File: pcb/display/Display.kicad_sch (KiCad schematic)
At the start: 32 parts, among them J101 RJ45, J102 Screw Terminal 3.5mm, J103 01x08_Pin, P101 USB_C_Plug_USB2.0, Q101 2N7002, SW101 SW_4x3mm, SW102 SW_4x3mm, SW103 SW_4x3mm, SW104 SW_4x3mm, U101 TMP1075DSGR, U102 ESP32-S3-MINI-1U-N8

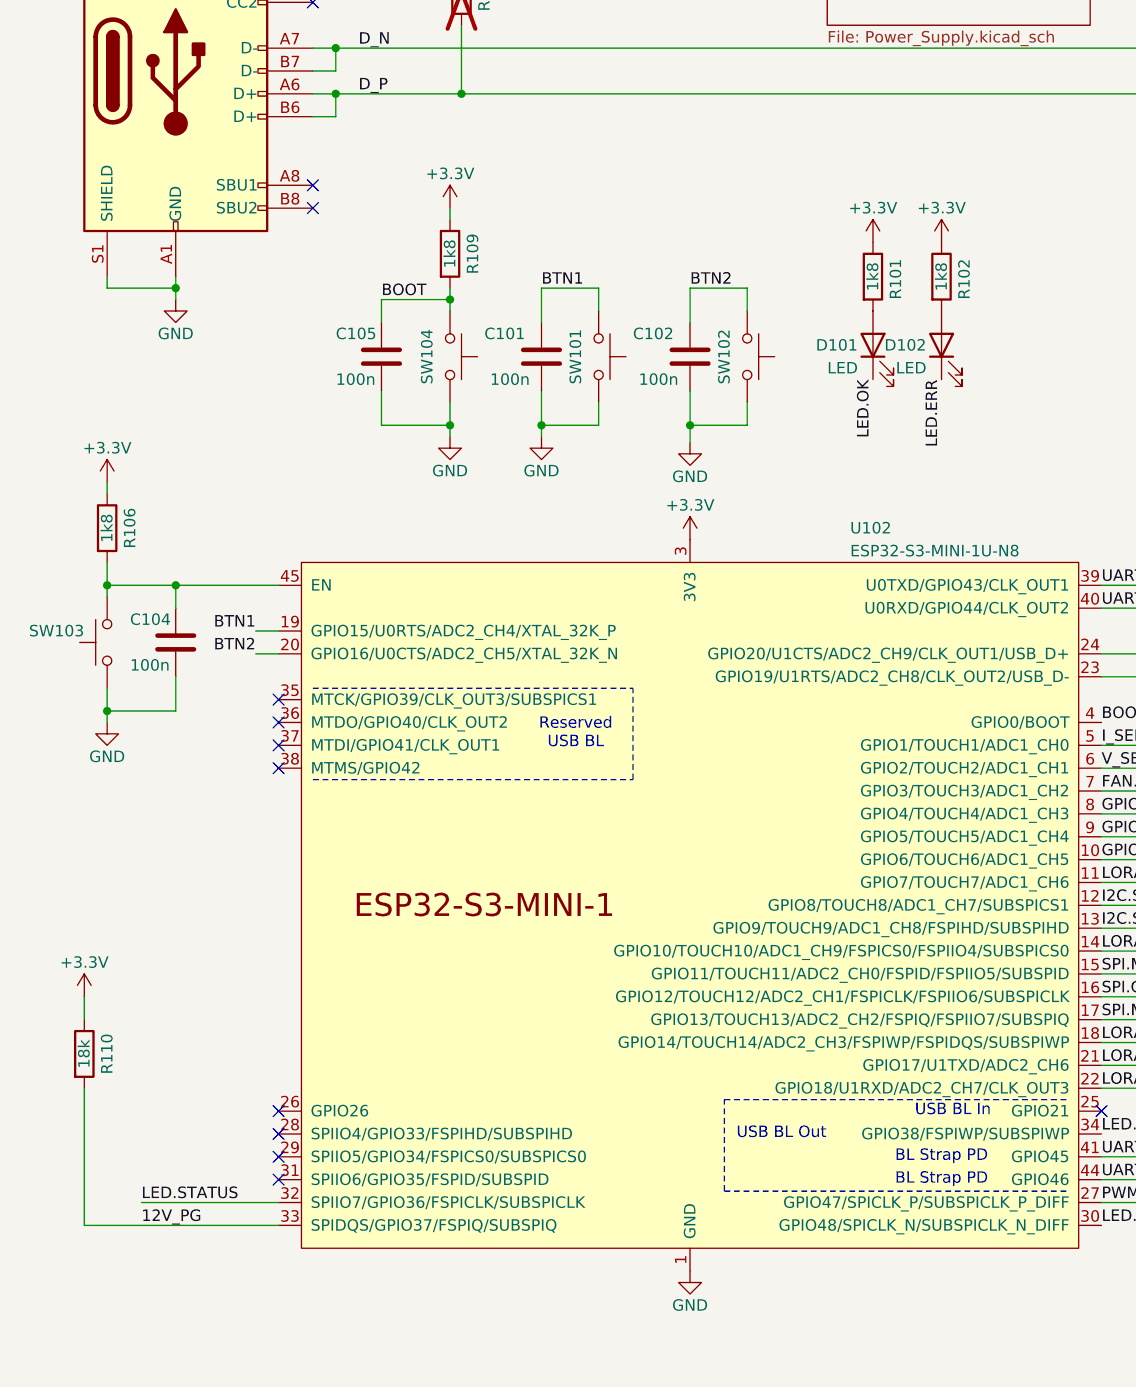
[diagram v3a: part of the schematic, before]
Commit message: Update some wrong values after import in JLC for production
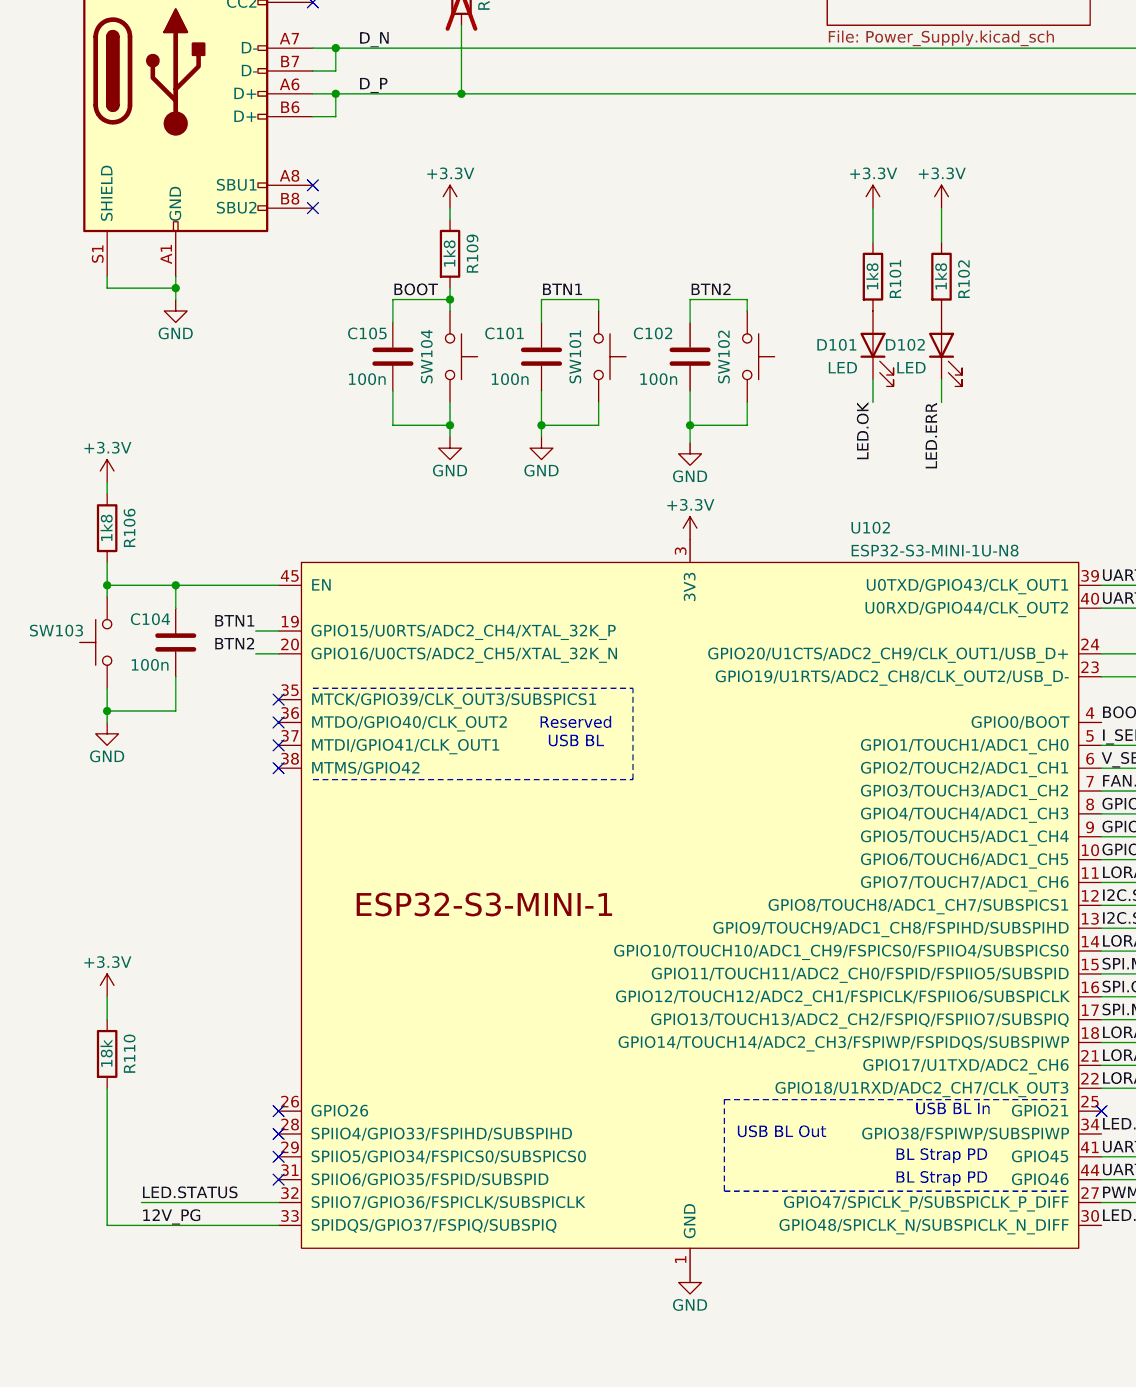
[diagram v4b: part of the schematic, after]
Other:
- moved on the sheet: C105, R110
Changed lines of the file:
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@@
 	(title_block
 		(title "Open Shot Clock - Display")
-		(date "2025-04-08")
+		(date "2025-04-11")
 		(rev "01")
 		(company "Ravenspark")
@@
 	(wire
 		(pts
-			(xy 52.07 71.12) (xy 52.07 68.58)
+			(xy 53.34 71.12) (xy 53.34 68.58)
 		)
 		(stroke
@@
 	(wire
 		(pts
-			(xy 19.05 171.45) (xy 40.64 171.45)
+			(xy 21.59 171.45) (xy 40.64 171.45)
 		)
 		(stroke
@@
 	(wire
 		(pts
-			(xy 86.36 71.12) (xy 86.36 67.31)
+			(xy 86.36 71.12) (xy 86.36 68.58)
 		)
 		(stroke
@@
 	(wire
 		(pts
-			(xy 69.85 67.31) (xy 69.85 71.12)
+			(xy 69.85 68.58) (xy 69.85 71.12)
 		)
 		(stroke
@@
 	(wire
 		(pts
+			(xy 106.68 58.42) (xy 106.68 62.23)
+		)
+		(stroke
+			(width 0)
+			(type default)
+		)
+	)
+	(wire
+		(pts
 			(xy 59.69 80.01) (xy 59.69 82.55)
 		)
@@
 	(wire
 		(pts
+			(xy 114.3 80.01) (xy 114.3 77.47)
+		)
+		(stroke
+			(width 0)
+			(type default)
+		)
+	)
+	(wire
+		(pts
 			(xy 146.05 110.49) (xy 132.08 110.49)
 		)
@@
 	(wire
 		(pts
-			(xy 76.2 67.31) (xy 69.85 67.31)
+			(xy 76.2 68.58) (xy 69.85 68.58)
 		)
 		(stroke
@@
 	(wire
 		(pts
-			(xy 19.05 156.21) (xy 19.05 171.45)
+			(xy 21.59 156.21) (xy 21.59 171.45)
 		)
 		(stroke
@@
 	(wire
 		(pts
-			(xy 59.69 68.58) (xy 52.07 68.58)
+			(xy 59.69 68.58) (xy 53.34 68.58)
 		)
 		(stroke
@@
 	(wire
 		(pts
-			(xy 92.71 67.31) (xy 92.71 69.85)
+			(xy 92.71 68.58) (xy 92.71 69.85)
 		)
 		(stroke
@@
 	(wire
 		(pts
-			(xy 76.2 69.85) (xy 76.2 67.31)
+			(xy 76.2 69.85) (xy 76.2 68.58)
 		)
 		(stroke
@@
 	(wire
 		(pts
-			(xy 19.05 146.05) (xy 19.05 148.59)
+			(xy 21.59 146.05) (xy 21.59 148.59)
 		)
 		(stroke
@@
 	(wire
 		(pts
+			(xy 114.3 58.42) (xy 114.3 62.23)
+		)
+		(stroke
+			(width 0)
+			(type default)
+		)
+	)
+	(wire
+		(pts
 			(xy 146.05 40.64) (xy 146.05 110.49)
 		)
@@
 	(wire
 		(pts
+			(xy 106.68 80.01) (xy 106.68 77.47)
+		)
+		(stroke
+			(width 0)
+			(type default)
+		)
+	)
+	(wire
+		(pts
 			(xy 266.7 134.62) (xy 266.7 128.27)
 		)
@@
 	(wire
 		(pts
-			(xy 52.07 78.74) (xy 52.07 82.55)
+			(xy 53.34 78.74) (xy 53.34 82.55)
 		)
 		(stroke
@@
 	(wire
 		(pts
-			(xy 86.36 67.31) (xy 92.71 67.31)
+			(xy 86.36 68.58) (xy 92.71 68.58)
 		)
 		(stroke
@@
 	(wire
 		(pts
-			(xy 59.69 82.55) (xy 52.07 82.55)
+			(xy 59.69 82.55) (xy 53.34 82.55)
 		)
 		(stroke
@@
 	)
 	(label "BTN1"
-		(at 69.85 67.31 0)
+		(at 69.85 68.58 0)
 		(fields_autoplaced yes)
 		(effects
@@
 	)
 	(label "LED.OK"
-		(at 106.68 77.47 270)
+		(at 106.68 80.01 270)
 		(fields_autoplaced yes)
 		(effects
@@
 	)
 	(label "LED.ERR"
-		(at 114.3 77.47 270)
+		(at 114.3 80.01 270)
 		(fields_autoplaced yes)
 		(effects
@@
 	)
 	(label "BTN2"
-		(at 86.36 67.31 0)
+		(at 86.36 68.58 0)
 		(fields_autoplaced yes)
 		(effects
@@
 	)
 	(label "BOOT"
-		(at 52.07 68.58 0)
+		(at 53.34 68.58 0)
 		(fields_autoplaced yes)
 		(effects
@@
 	(symbol
 		(lib_id "Device:R")
-		(at 19.05 152.4 0)
+		(at 21.59 152.4 0)
 		(unit 1)
 		(exclude_from_sim no)
@@
 		(dnp no)
 		(property "Reference" "R110"
-			(at 21.59 152.4 90)
+			(at 24.13 152.4 90)
 			(effects
 				(font
@@
 		)
 		(property "Value" "18k"
-			(at 19.05 152.4 90)
+			(at 21.59 152.4 90)
 			(effects
 				(font
@@
 		)
 		(property "Footprint" "Resistor_SMD:R_0402_1005Metric"
-			(at 17.272 152.4 90)
+			(at 19.812 152.4 90)
 			(effects
 				(font
@@
 		)
 		(property "Datasheet" "~"
-			(at 19.05 152.4 0)
+			(at 21.59 152.4 0)
 			(effects
 				(font
@@
 		)
 		(property "Description" "Resistor"
-			(at 19.05 152.4 0)
+			(at 21.59 152.4 0)
 			(effects
 				(font
@@
 	(symbol
 		(lib_id "power:+3.3V")
-		(at 114.3 62.23 0)
+		(at 114.3 58.42 0)
 		(unit 1)
 		(exclude_from_sim no)
@@
 		(dnp no)
 		(property "Reference" "#PWR0102"
-			(at 114.3 66.04 0)
+			(at 114.3 62.23 0)
 			(effects
 				(font
@@
 		)
 		(property "Value" "+3.3V"
-			(at 114.3 58.42 0)
+			(at 114.3 54.61 0)
 			(effects
 				(font
@@
 		)
 		(property "Footprint" ""
-			(at 114.3 62.23 0)
+			(at 114.3 58.42 0)
 			(effects
 				(font
@@
 		)
 		(property "Datasheet" ""
-			(at 114.3 62.23 0)
+			(at 114.3 58.42 0)
 			(effects
 				(font
@@
 		)
 		(property "Description" "Power symbol creates a global label with name \"+3.3V\""
-			(at 114.3 62.23 0)
+			(at 114.3 58.42 0)
 			(effects
 				(font
@@
 	(symbol
 		(lib_id "Device:C")
-		(at 52.07 74.93 0)
+		(at 53.34 74.93 0)
 		(unit 1)
 		(exclude_from_sim no)
@@
 		(dnp no)
 		(property "Reference" "C105"
-			(at 46.99 72.39 0)
+			(at 48.26 72.39 0)
 			(effects
 				(font
@@
 		)
 		(property "Value" "100n"
-			(at 46.99 77.47 0)
+			(at 48.26 77.47 0)
 			(effects
 				(font
@@
 		)
 		(property "Footprint" "Capacitor_SMD:C_0402_1005Metric"
-			(at 53.0352 78.74 0)
+			(at 54.3052 78.74 0)
 			(effects
 				(font
@@
 		)
 		(property "Datasheet" "~"
-			(at 52.07 74.93 0)
+			(at 53.34 74.93 0)
 			(effects
 				(font
@@
 		)
 		(property "Description" "Unpolarized capacitor"
-			(at 52.07 74.93 0)
+			(at 53.34 74.93 0)
 			(effects
 				(font
@@
 		)
 		(property "JLC PN" "C307331"
-			(at 52.07 74.93 0)
+			(at 53.34 74.93 0)
 			(effects
 				(font
@@
 	(symbol
 		(lib_id "power:+3.3V")
-		(at 106.68 62.23 0)
+		(at 106.68 58.42 0)
 		(unit 1)
 		(exclude_from_sim no)
@@
 		(dnp no)
 		(property "Reference" "#PWR0101"
-			(at 106.68 66.04 0)
+			(at 106.68 62.23 0)
 			(effects
 				(font
@@
 		)
 		(property "Value" "+3.3V"
-			(at 106.68 58.42 0)
+			(at 106.68 54.61 0)
 			(effects
 				(font
@@
 		)
 		(property "Footprint" ""
-			(at 106.68 62.23 0)
+			(at 106.68 58.42 0)
 			(effects
 				(font
@@
 		)
 		(property "Datasheet" ""
-			(at 106.68 62.23 0)
+			(at 106.68 58.42 0)
 			(effects
 				(font
@@
 		)
 		(property "Description" "Power symbol creates a global label with name \"+3.3V\""
-			(at 106.68 62.23 0)
+			(at 106.68 58.42 0)
 			(effects
 				(font
@@
 	(symbol
 		(lib_id "power:+3.3V")
-		(at 19.05 146.05 0)
+		(at 21.59 146.05 0)
 		(unit 1)
 		(exclude_from_sim no)
@@
 		(dnp no)
 		(property "Reference" "#PWR0127"
-			(at 19.05 149.86 0)
+			(at 21.59 149.86 0)
 			(effects
 				(font
@@
 		)
 		(property "Value" "+3.3V"
-			(at 19.05 142.24 0)
+			(at 21.59 142.24 0)
 			(effects
 				(font
@@
 		)
 		(property "Footprint" ""
-			(at 19.05 146.05 0)
+			(at 21.59 146.05 0)
 			(effects
 				(font
@@
 		)
 		(property "Datasheet" ""
-			(at 19.05 146.05 0)
+			(at 21.59 146.05 0)
 			(effects
 				(font
@@
 		)
 		(property "Description" "Power symbol creates a global label with name \"+3.3V\""
-			(at 19.05 146.05 0)
+			(at 21.59 146.05 0)
 			(effects
 				(font

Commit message: Update component values after feedback from JLC
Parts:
- SW101, SW102, SW103, SW104: JLC PN C18078117 -> C18077679
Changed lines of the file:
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@@
 			)
 		)
-		(property "JLC PN" "C18078117"
+		(property "JLC PN" "C18077679"
 			(at 92.71 74.93 0)
 			(effects
@@
 			)
 		)
-		(property "JLC PN" "C18078117"
+		(property "JLC PN" "C18077679"
 			(at 21.59 106.68 0)
 			(effects
@@
 			)
 		)
-		(property "JLC PN" "C18078117"
+		(property "JLC PN" "C18077679"
 			(at 59.69 74.93 0)
 			(effects
@@
 			)
 		)
-		(property "JLC PN" "C18078117"
+		(property "JLC PN" "C18077679"
 			(at 76.2 74.93 0)
 			(effects
